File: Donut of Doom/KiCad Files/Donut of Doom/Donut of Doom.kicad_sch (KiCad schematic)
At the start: 2 parts

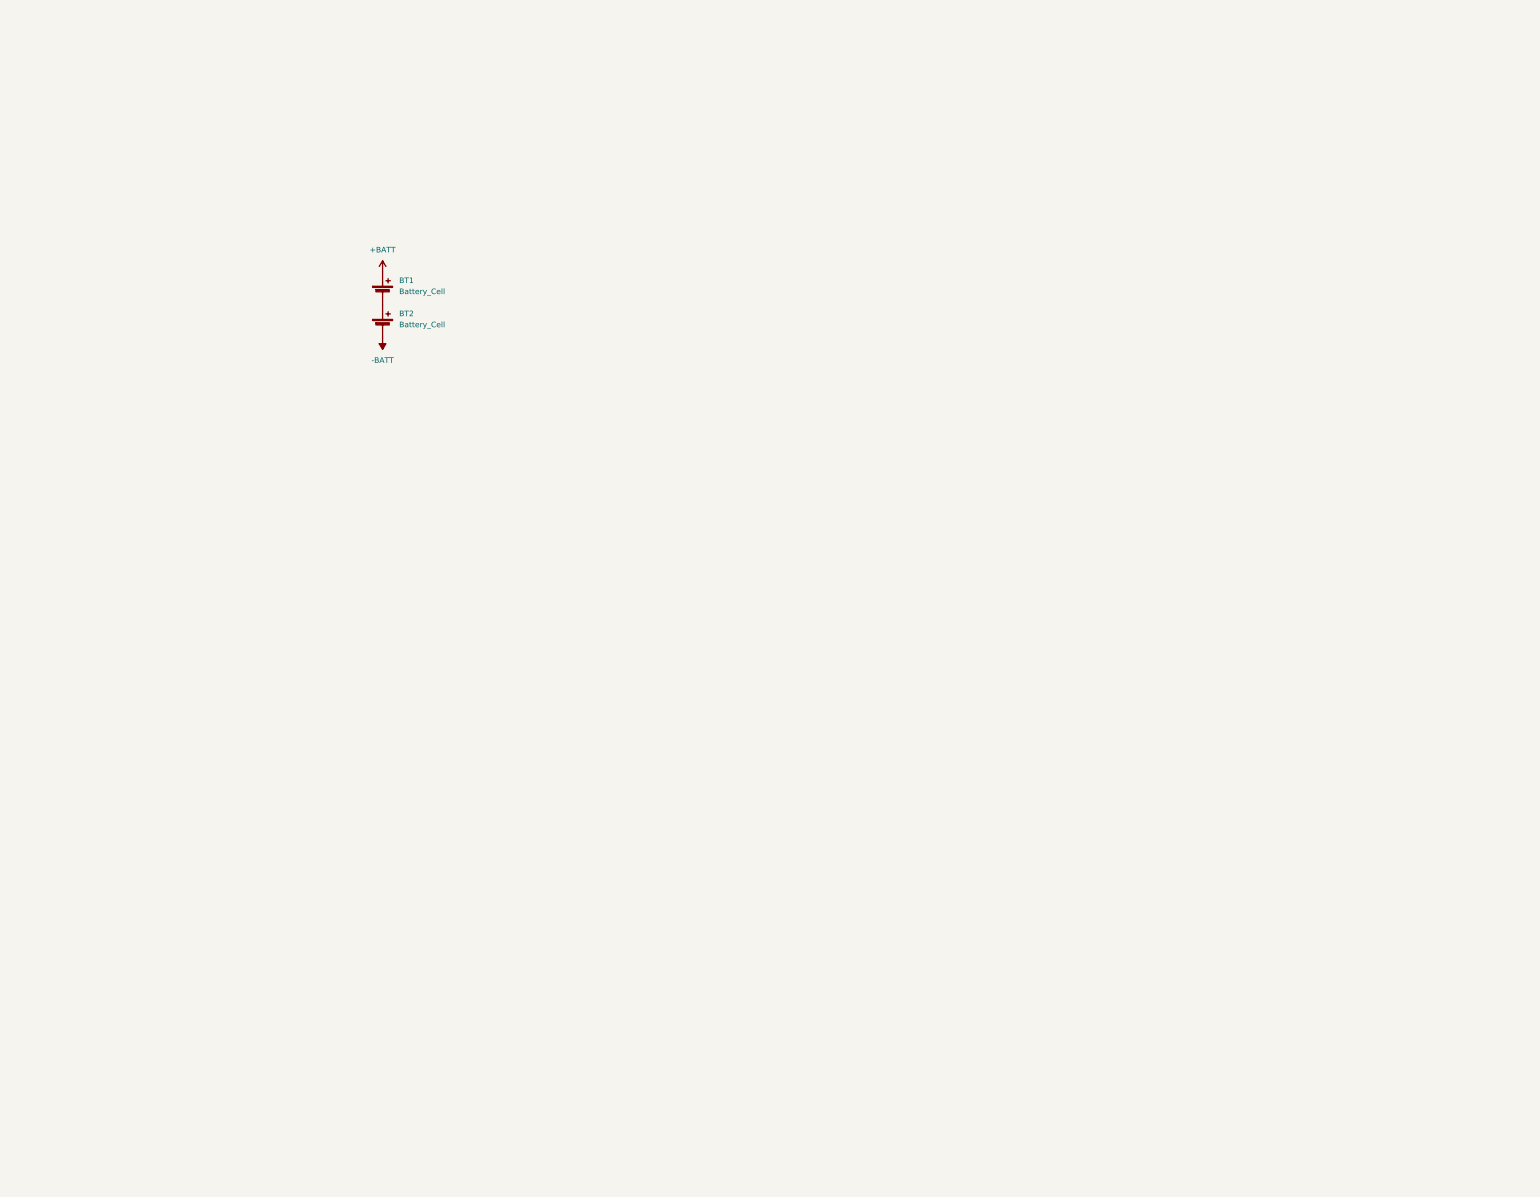
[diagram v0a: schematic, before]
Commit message: Added Custom Symbol Library and worked more on Schematic
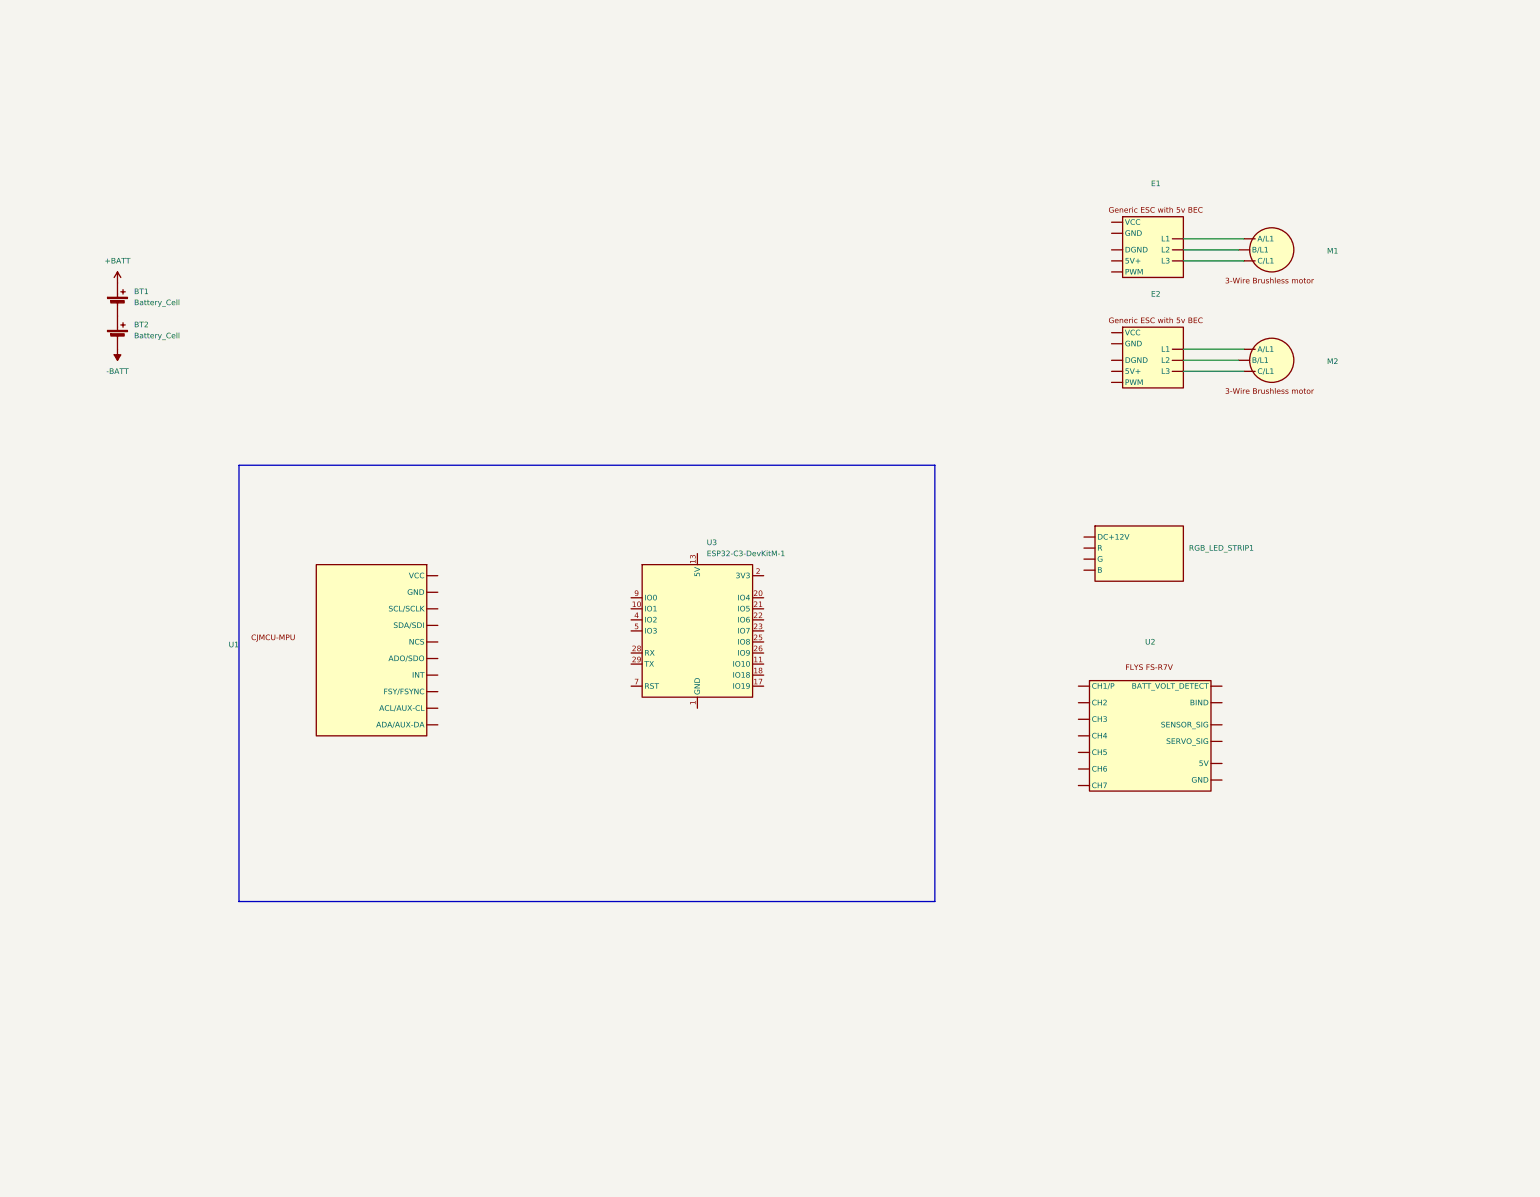
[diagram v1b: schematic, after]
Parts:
- added E1, E2: ~, symbol Battlebots Symbols:ESC_30A_Generic_with_5V_BEC
- added M1, M2: ~, symbol Battlebots Symbols:Generic_3_Wire_Brushless_motor
- added RGB_LED_STRIP1: ~, symbol Battlebots Symbols:LED_Strip
- added U1: ~, symbol Battlebots Symbols:CJMCU-MPU
- added U2: ~, symbol Battlebots Symbols:FLYS_FS-R7V
- added U3: ESP32-C3-DevKitM-1, RF_Module:ESP32-C3-DevKitM-1, symbol RF_Module:ESP32-C3-DevKitM-1
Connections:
- new net: E1. (L3), M1. (C/L1) (x3)
- new net: E2. (L3), M2. (C/L1) (x3)
- new net: U3.1 (GND), U3.12 (GND), U3.15 (GND), U3.16 (GND), U3.19 (GND), U3.24 (GND), U3.27 (GND), U3.30 (GND), U3.6 (GND), U3.8 (GND)
- new net: U3.13 (5V), U3.14 (5V)
- new net: U3.2 (3V3), U3.3 (3V3)
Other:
- moved on the sheet: BT1, BT2

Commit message: Started a lot of work on DOD V2 PCB with the Pico 2
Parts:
- removed E1, E2: ~, symbol Battlebots Symbols:ESC_30A_Generic_with_5V_BEC
- removed RGB_LED_STRIP1: ~, symbol Battlebots Symbols:LED_Strip
- removed U2: ~, symbol Battlebots Symbols:FLYS_FS-R7V
- removed U3: ESP32-C3-DevKitM-1, RF_Module:ESP32-C3-DevKitM-1, symbol RF_Module:ESP32-C3-DevKitM-1
- added A1: RaspberryPi_Pico, Module_RaspberryPi_Pico:RaspberryPi_Pico_Original_SMD_HandSolder, symbol MCU_Module_RaspberryPi_Pico:RaspberryPi_Pico_DebugPins
- added D1: LED, symbol Device:LED
- added D2, D3: D_TVS, symbol Device:D_TVS
- added ESC1, ESC2: ~, symbol Battlebots Symbols:jcr_rc_mini_35A_am32
- added SW1: ~, symbol Battlebots Symbols:FingerTech_Power_Switch
- added U2: ~, symbol Battlebots Symbols:5V_Stepdown_module
- added U3: ~, Battlebots:BetaFPV ExpressLRS Reciever Lite V1.2, symbol Battlebots Symbols:BETAFPV_ExpressLRS_Lite_V1.2
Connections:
- net +BATT: now also ESC1. (C), ESC2. (C), U2.1 (Input+)
- net -BATT: now also ESC1. (C), ESC2. (C), SW1. (NC), U2.2 (Input-); no longer BT2.2 (-)
- net at M1. (C/L1): now also ESC1. (C)
- net at M2. (C/L1): now also ESC2. (C)
- net I2C0 SDA: now reaches U1. (GND)
- net I2C0 SDA: now also A1.11 (GPIO8)
- new net: A1.1 (GPIO0), U3.1 (RX)
- new net: A1.2 (GPIO1), U3.2 (TX)
- new net: A1.5 (GPIO3), D1.2 (A)
- new net: ESC1. (C), M1. (C/L1) (x2)
- new net: ESC2. (C), M2. (C/L1) (x2)
- new net: D2.2 (A2), ESC2. (C)
- new net: BT2.2 (-), SW1. (NC)
- new net: D3.2 (A2), ESC1. (C)
- new net +3V3: A1.36 (3V3), U1. (GND)
- new net +5V: A1.39 (VSYS), U2.4 (5v+), U3.3 (5V+)
- new net ESC1 PWM: A1.25 (GPIO19), D3.1 (A1)
- new net ESC2 PWM: A1.26 (GPIO20), D2.1 (A1)
- new net GND: A1.13 (GND), A1.18 (GND), A1.23 (GND), A1.28 (GND), A1.3 (GND), A1.33 (AGND), A1.38 (GND), A1.8 (GND), A1.D2 (GND), D1.1 (K), ESC1. (C), ESC2. (C), U1. (GND), U2.3 (5v-), U3.4 (GND)
- new net I2C0 SCL: A1.12 (GPIO9), U1. (GND)
- no-connect marks 0 -> 9
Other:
- note added: "ESCS"
- note added: "LOGIC AND LEDS"
- note added: "POWER"
- note added: "Pico 2 has a 5v to 3V3 regulator"
- note added: "UART0 RX"
- note added: "UART0 TX"
- moved on the sheet: BT1, BT2, M1, M2, U1

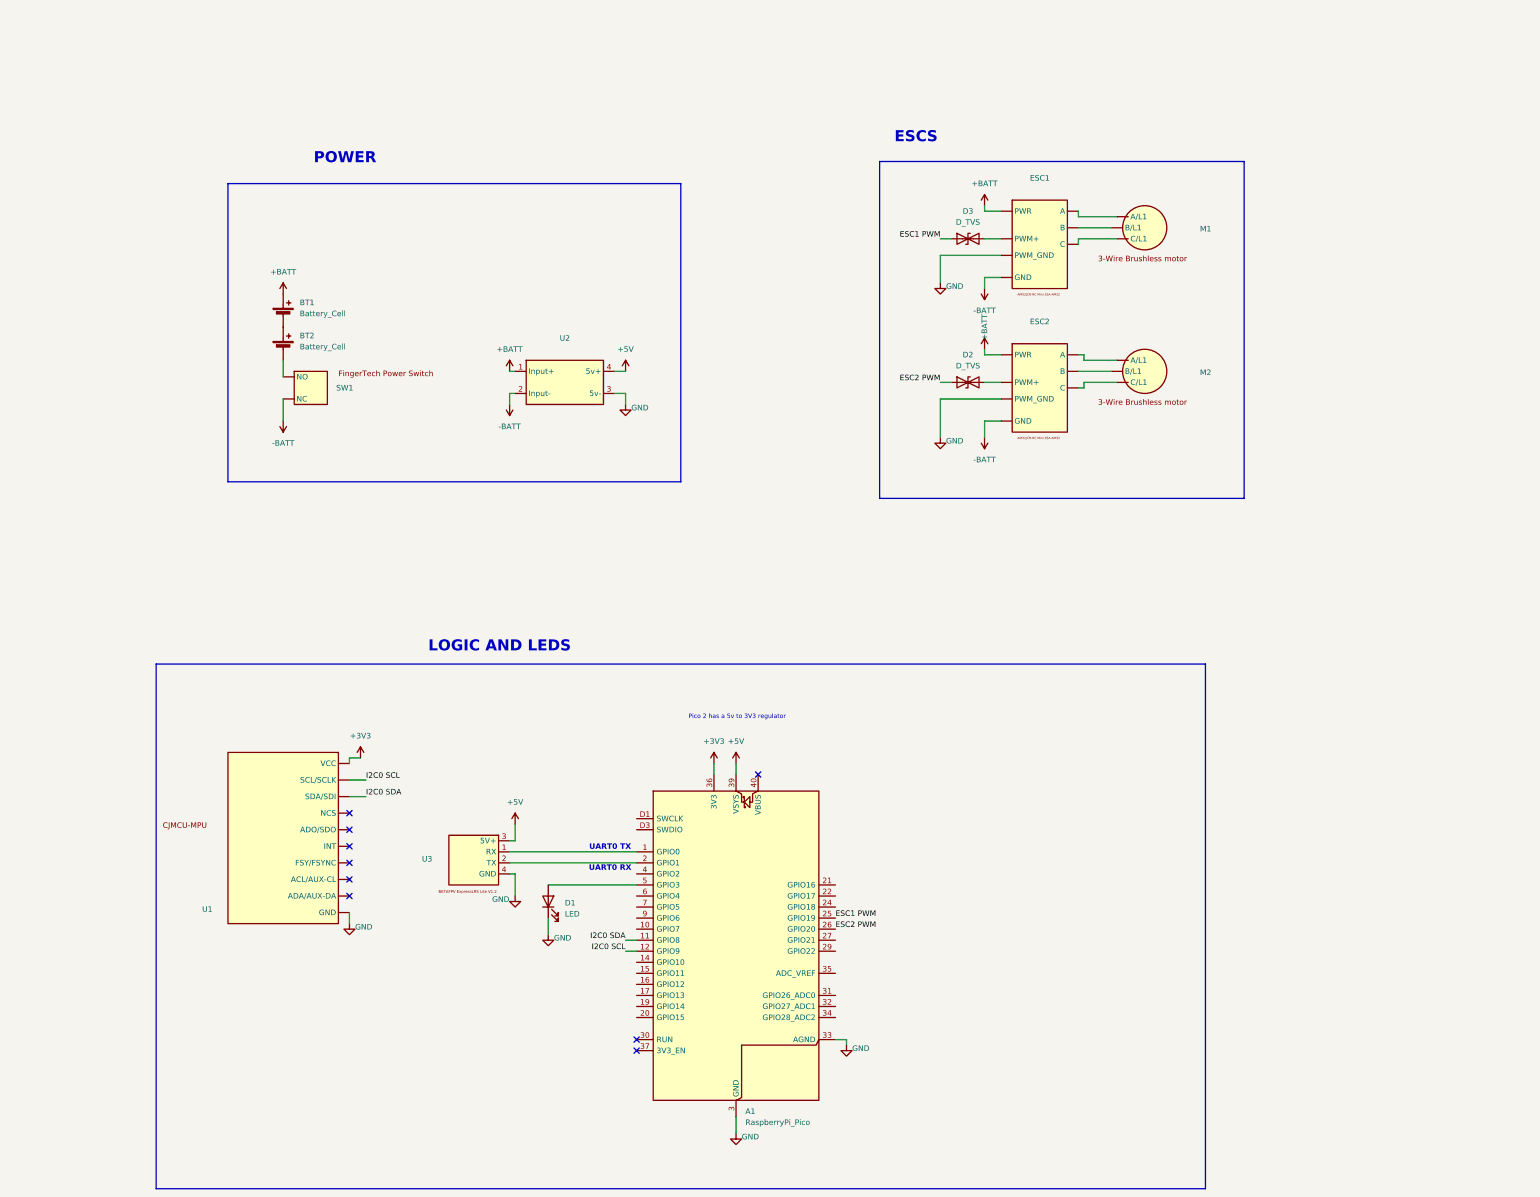
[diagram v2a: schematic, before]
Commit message: Added voltage spike protection circuitry to ESCs
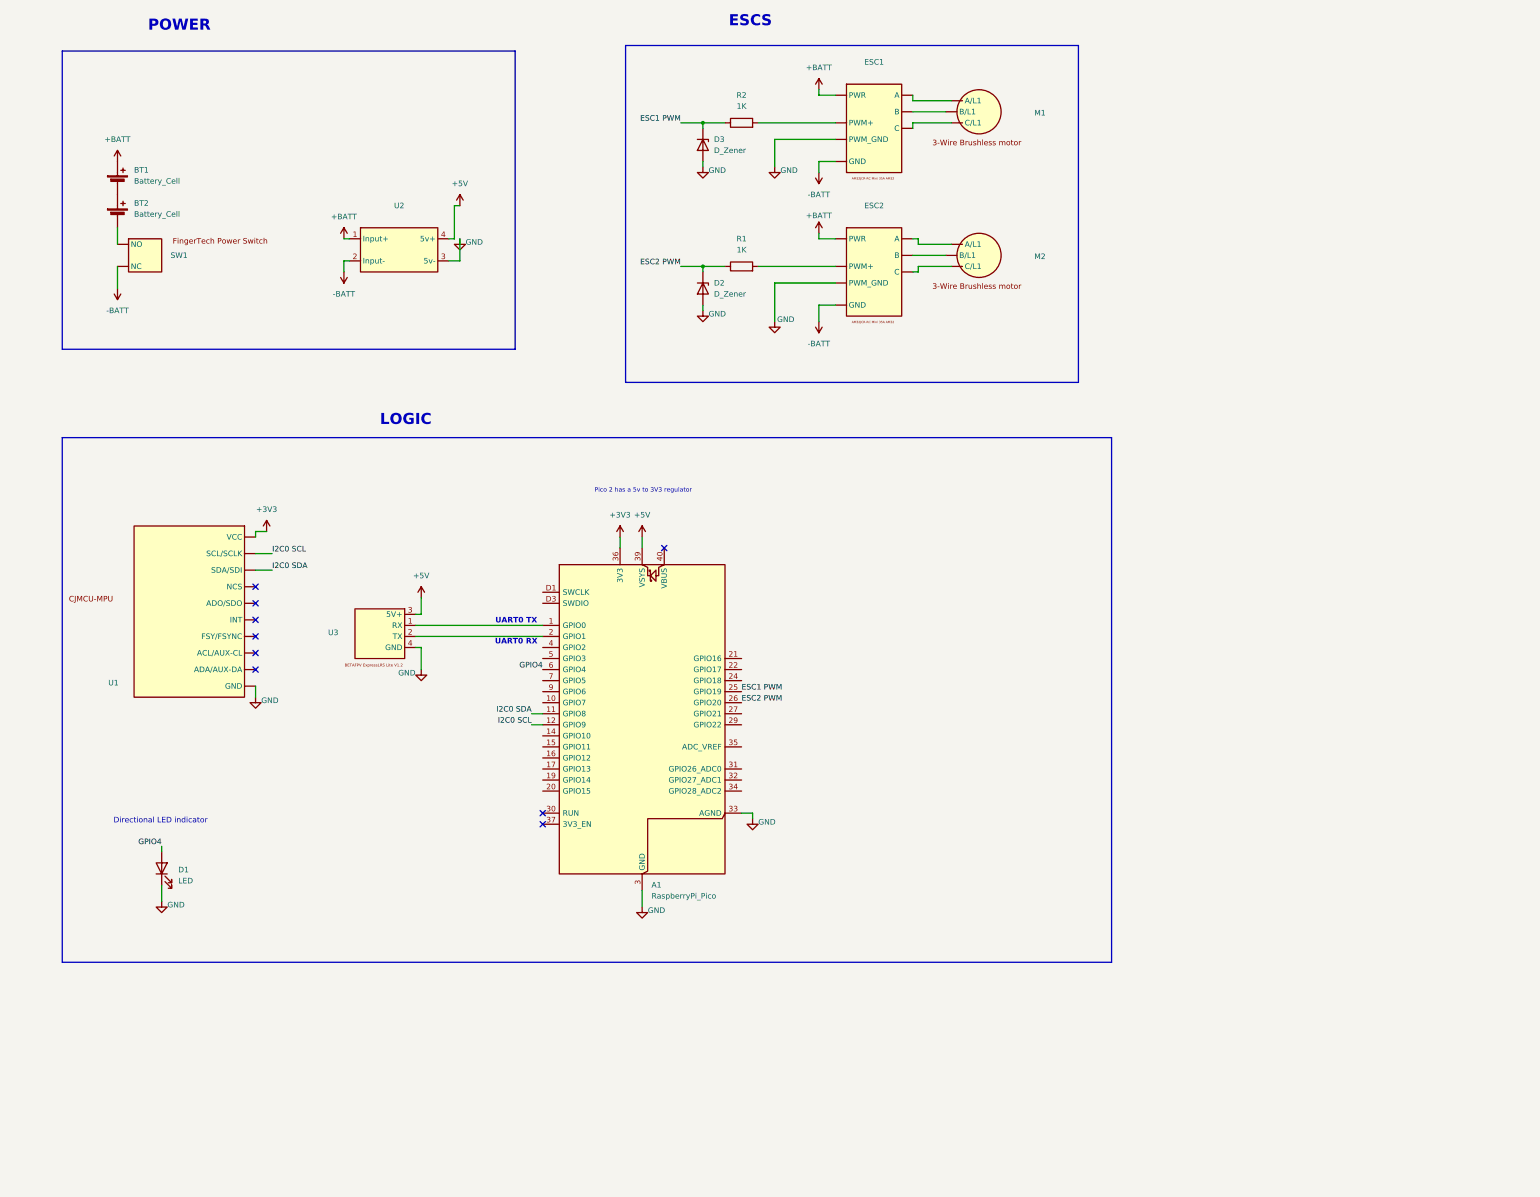
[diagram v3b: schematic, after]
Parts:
- removed D2, D3: D_TVS, symbol Device:D_TVS
- added D2, D3: D_Zener, Diode_SMD:D_MicroSMP_KA, symbol Device:D_Zener
- added R1, R2: 1K, Resistor_SMD:R_0603_1608Metric_Pad0.98x0.95mm_HandSolder, symbol Device:R
- U2: footprint (none) -> Battlebots:5V_Stepdown_module
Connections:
- net ESC1 PWM: now also D3.1 (K), R2.1
- net ESC2 PWM: now also D2.1 (K), R1.1
- net GND: now also D2.2 (A), D3.2 (A)
- net at A1.5 (GPIO3): no longer D1.2 (A)
- net GPIO4: now reaches A1.6 (GPIO4)
- net GPIO4: now also D1.2 (A)
- new net: ESC2. (C), R1.2
- new net: ESC1. (C), M1. (C/L1) (x2)
- new net: ESC2. (C), M2. (C/L1) (x2)
- new net: ESC1. (C), R2.2
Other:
- note added: "Directional LED indicator"
- note added: "LOGIC"
- note removed: "LOGIC AND LEDS"
- moved on the sheet: A1, BT1, BT2, D1, ESC1, ESC2, M1, M2, SW1, U1, U2, U3

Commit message: fixed accel pins
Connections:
- new net: ESC1. (C), M1. (C/L1) (x2)
- new net: ESC2. (C), M2. (C/L1) (x2)
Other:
- note added: "Directional LED indicator (mutable)"
- note removed: "Directional LED indicator"
- moved on the sheet: U1
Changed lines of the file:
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@@
 	(rectangle
 		(start 21.59 115.57)
-		(end 262.89 236.22)
+		(end 262.89 241.3)
 		(stroke
 			(width 0)
@@
 		)
 	)
-	(text "Directional LED indicator\n"
+	(text "Directional LED indicator (mutable)\n\n"
 		(exclude_from_sim no)
 		(at 44.196 203.708 0)
@@
 	)
 	(image
-		(at 220.98 222.25)
+		(at 227.33 227.33)
 		(data "iVBORw0KGgoAAAANSUhEUgAAA1AAAAFFCAIAAABt/ZtnAAAAA3NCSVQICAjb4U/gAAAgAElEQVR4"
 			"nOy9ebwkVXk+/r5nq6277zYzDDAsBgLIIoiKjAsa9KcQBBVRQbYYRUgMagRjUBT3LQiiaBBBFCPu"
